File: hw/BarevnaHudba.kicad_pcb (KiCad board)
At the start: 2 copper layers, 80 x 30 mm, 58 parts, among them J1 USB, J2 Conn_01x04_Male, J3 Conn_01x06, Q1 BC817, Q2 BC817, Q3 BC817, U1 NE5532, U2 NE5532

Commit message: Initial layout of PCB
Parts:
- C5, C6, C7, C8, D2, D3, R10, R11, R12, R13, R16, R17, R18, R19, R6, R7, U2: moved to B.Cu
- moved R6 97.1 mm to (88.8, 59.0), turned to 90 degrees
- moved R11 88.7 mm to (97.0, 66.0)
- moved R10 88.0 mm to (90.5, 66.0)
- moved R7 83.5 mm to (88.8, 72.0), turned to 270 degrees
- moved C5 83.5 mm to (92.7, 59.0), turned to 270 degrees
- moved R16 80.8 mm to (100.5, 59.0), turned to 270 degrees
- moved R13 79.7 mm to (105.5, 74.2), turned to 270 degrees
- moved C8 77.2 mm to (96.0, 72.0), turned to 270 degrees
- moved R17 74.8 mm to (104.2, 59.0), turned to 90 degrees
- moved C6 71.3 mm to (96.5, 59.0), turned to 90 degrees
- moved R12 68.7 mm to (101.7, 74.2), turned to 90 degrees
- moved C7 64.6 mm to (92.3, 72.0), turned to 90 degrees
- moved R19 63.1 mm to (113.2, 74.2), turned to 270 degrees
- moved C11 56.4 mm to (104.2, 58.2), turned to 270 degrees
- moved R18 56.1 mm to (109.3, 74.2), turned to 90 degrees
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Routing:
- net VCC: track 0.00 -> 35.3 mm
- net Net-(C3-Pad2): track 0.00 -> 31.9 mm
- net GND: track 0.00 -> 31.1 mm
- net Net-(R14-Pad2): track 0.00 -> 13.5 mm
- net Net-(J1-Pad2): track 0.00 -> 8.92 mm
- net Net-(J1-Pad3): track 0.00 -> 8.91 mm
- net Net-(R3-Pad2): track 0.00 -> 7.98 mm
- net Net-(R2-Pad1): track 0.00 -> 7.72 mm
- net input: track 0.00 -> 7.21 mm
- net Net-(C2-Pad1): track 0.00 -> 5.58 mm
- net Net-(C3-Pad1): track 0.00 -> 5.08 mm
- net Net-(C9-Pad1): track 0.00 -> 4.31 mm
- net Net-(C1-Pad1): track 0.00 -> 3.41 mm
- net signal: track 0.00 -> 3.12 mm

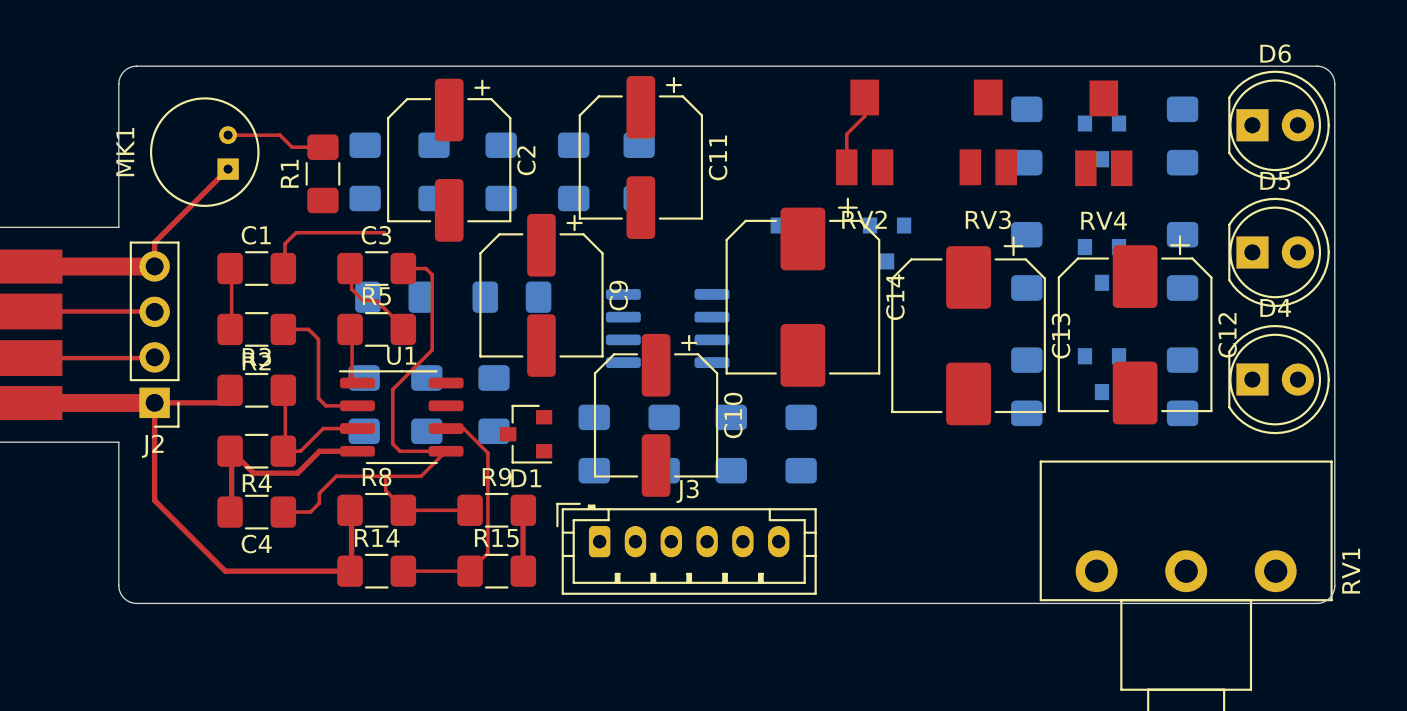
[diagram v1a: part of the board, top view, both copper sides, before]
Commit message: Add switch, improve layout and silkscreen
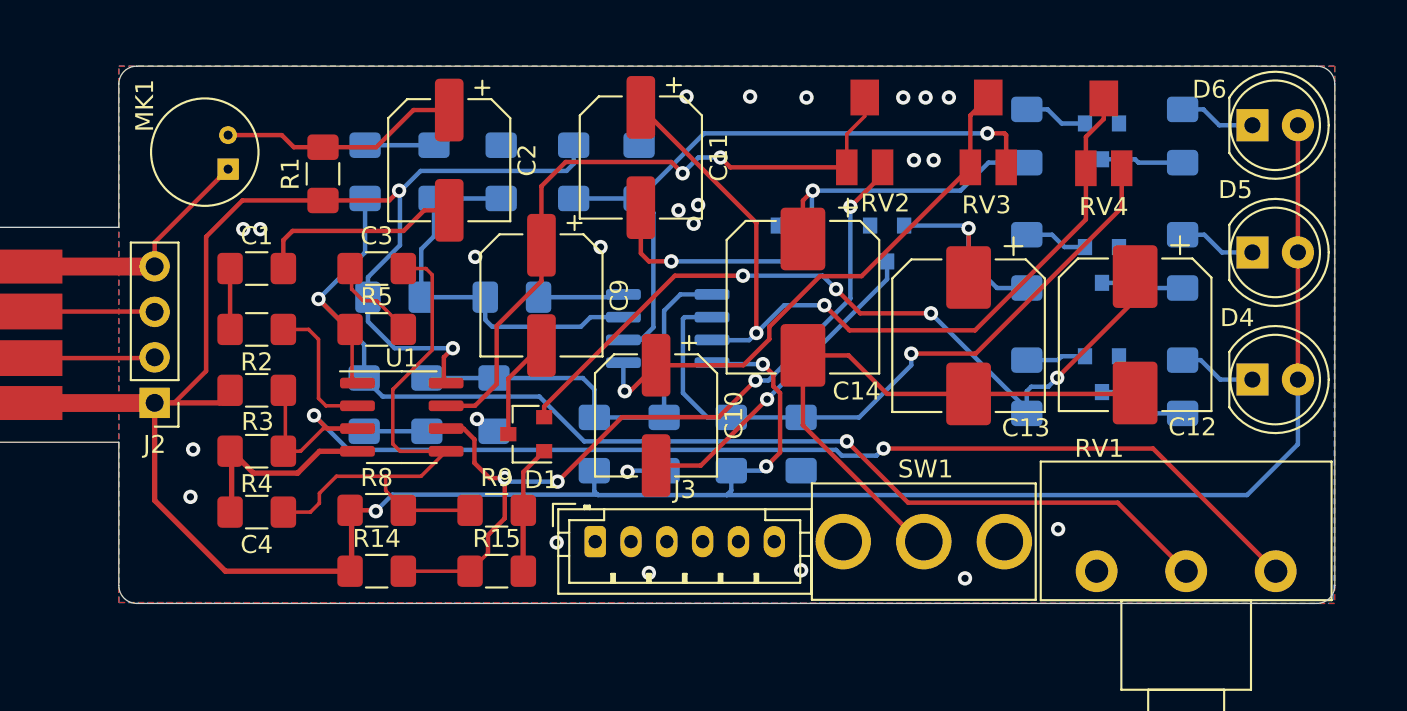
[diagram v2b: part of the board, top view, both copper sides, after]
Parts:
- added SW1: SW_SPDT, hw:KNX-1, F.Cu at (120.0, 79.7)
- moved J3 0.25 mm to (101.7, 79.7)
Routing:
- net VCC: track 35.3 -> 171.8 mm, vias 0 -> 5
- net signal: track 3.12 -> 68.1 mm, vias 0 -> 2
- net Net-(R3-Pad2): track 7.98 -> 68.3 mm, vias 0 -> 2
- net Net-(C11-Pad1): track 0.00 -> 47.3 mm, vias 0 -> 2
- net Net-(C12-Pad1): track 0.00 -> 44.6 mm, vias 0 -> 4
- net Net-(R18-Pad2): track 0.00 -> 38.3 mm, vias 0 -> 1
- net Net-(R16-Pad2): track 0.00 -> 37.0 mm, vias 0 -> 1
- net Net-(C9-Pad1): track 4.31 -> 38.2 mm, vias 0 -> 2
- net Net-(R14-Pad2): track 13.5 -> 47.1 mm, vias 0 -> 4
- net stroboscope_en: track 0.00 -> 32.6 mm
- net Net-(C10-Pad1): track 0.00 -> 30.8 mm, vias 0 -> 1
- net Net-(C7-Pad2): track 0.00 -> 24.1 mm
- net Net-(C5-Pad2): track 0.00 -> 22.5 mm
- net Net-(C10-Pad2): track 0.00 -> 18.2 mm, vias 0 -> 1
- net Net-(C14-Pad1): track 0.00 -> 17.5 mm, vias 0 -> 1
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- added copper zone on B.Cu, net GND
- added copper zone on F.Cu, net GND
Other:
- board text added: "BarevnaHudba v0.1 MAK 11/2020"
